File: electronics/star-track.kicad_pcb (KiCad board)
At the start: 2 copper layers, 142.2 x 61 mm, 25 parts, among them J4 AZ motor, J5 ALT motor, P1 Power in (from CB1 / J1), P2 Case: LEDs, buzzer, E-stop, P3 Hand unit (to J2), U1 L7805CV

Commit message: Drop the buzzer; colour the stripboard pictures by net
- Remove BZ1 and its GPIO from the schematic, the stripboard and the
  docs. Feedback at the mount is the two LEDs. P2 keeps five pads.
- Stripboard pictures: one colour per net for the strips and the wire
  links, fixed colours for GND, +12V, +3V3 and +5V.

Co-Authored-By: Claude Opus 5.5 <noreply@anthropic.com>
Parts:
- P2: value Case: LEDs, buzzer, E-stop -> Case: LEDs, E-stop
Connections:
- A1 pad 20: /BUZZER -> unconnected-(A1-GPIO14-Pad20)
- P2 pad 3: /BUZZER -> /EN_OUT
- P2 pad 4: /EN_OUT -> GND
- P2 pad 5: GND -> /DRV_EN
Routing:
- net unconnected-(A1-GPIO14-Pad20): track 0.00 -> 48.3 mm
- net /BUZZER: track 48.3 -> 0.00 mm

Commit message: Replace the L7805 with a DC-DC converter, add a GPS module
- U1 is now a DC-DC step-down module set to 5 V, off the board on three
  wires (pads P5). The L7805 and its heatsink are gone.
- GPS module GY-GPS6MV2 (u-blox NEO-6M) on GPIO16/17, powered from 5 V,
  wired to pads P4. It gives the time and the site to the firmware.
- Motor cables are soldered into J4, J5.
- Stripboard pictures: the notes under the board are laid out in columns.
- docs: power, GPS, pins, power budget and parts list updated.

Co-Authored-By: Claude Opus 5.5 <noreply@anthropic.com>
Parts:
- removed U1: L7805CV, Package_TO_SOT_THT:TO-220-3_Vertical
- added P4: GPS module (U2), Wire_pads, F.Cu at (191.4, 82.9)
- added P5: DC-DC module (U1), Wire_pads, F.Cu at (100.0, 90.5)
- moved W4 2.54 mm to (163.5, 98.1)
- moved W5 2.54 mm to (161.0, 87.9)
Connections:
- A1 pad 10: unconnected-(A1-GPIO17-Pad10) -> /GPS_TX
- A1 pad 9: unconnected-(A1-GPIO16-Pad9) -> /GPS_RX
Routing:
- net unconnected-(A1-GPIO17-Pad10): track 48.3 -> 0.00 mm
- net unconnected-(A1-GPIO16-Pad9): track 48.3 -> 0.00 mm
- net /GPS_TX: track 0.00 -> 48.3 mm
- net /GPS_RX: track 0.00 -> 48.3 mm

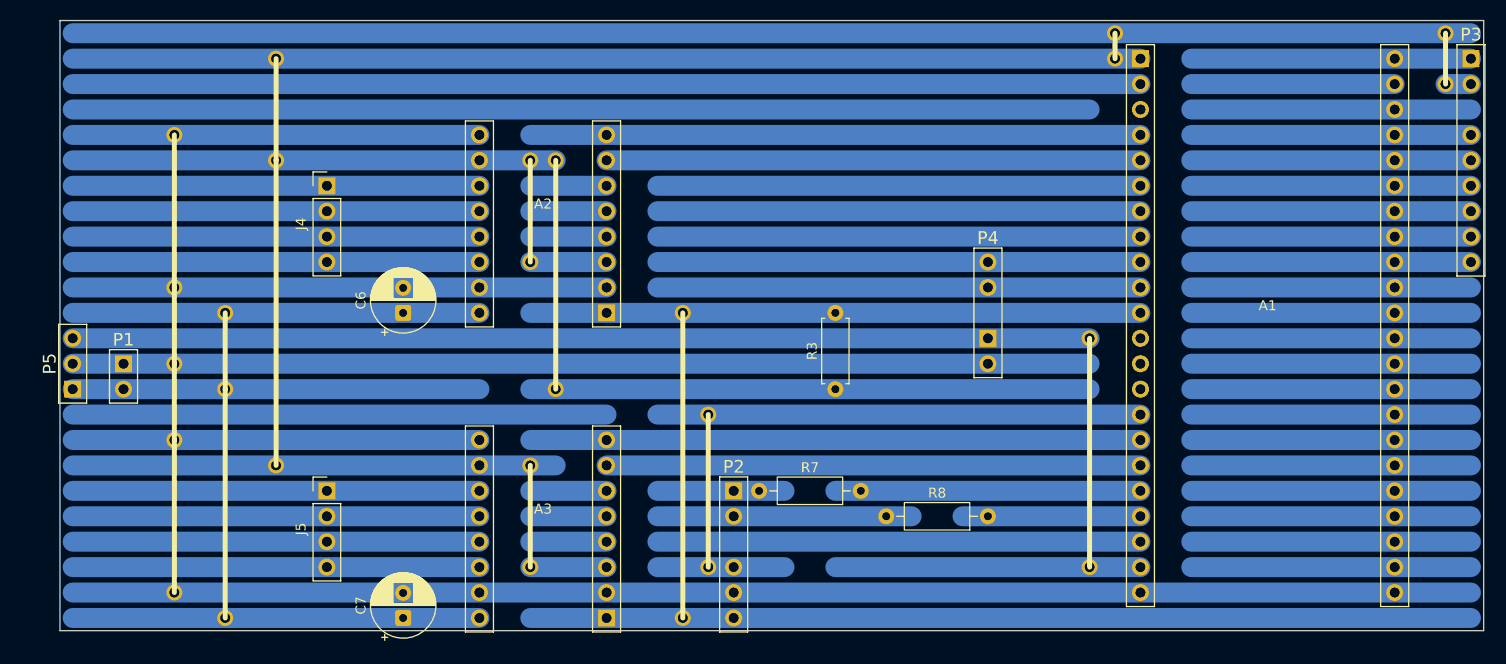
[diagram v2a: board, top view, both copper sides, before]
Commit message: Add a two-layer PCB for the electronics; move the stripboard to a subfolder
- electronics/star-track.kicad_pcb: 72 x 61 mm, two layers, through-hole
  parts only, rounded corners, four M3 holes. Laid out by function:
  motor wires and power on the left edge, drivers in the middle, the
  ESP32 board on the right with the resistors under it, hand unit and
  GPS on the right edge, LEDs and E-stop on the bottom edge (each LED
  with its own GND pad). Power input on a 5.08 mm screw terminal.
- Routed with Freerouting, GND fill on both layers except under the
  ESP32 antenna. DRC passes with no unconnected pads.
- Gerber and drill files for ordering, and renders of both sides.
- Net classes for the track widths; KiCad's default checks restored.
- ESP32 footprint courtyard limited to its two header strips.
- The stripboard moves to electronics/stripboard/.

Co-Authored-By: Claude Opus 5.5 <noreply@anthropic.com>
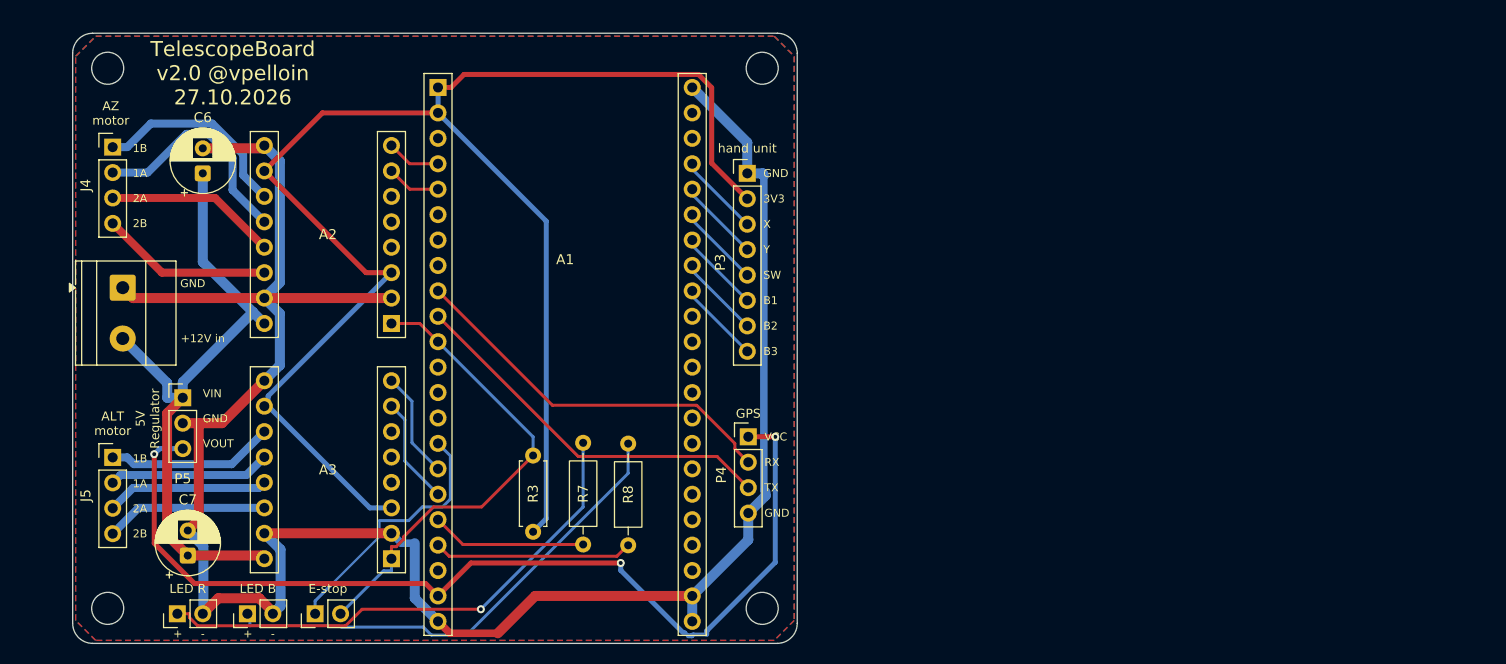
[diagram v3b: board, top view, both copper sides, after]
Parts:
- removed W1, W10, W11, W2, W3, W4, W5, W6, W7, W8, W9: Wire link, Wire_link
- added H1: MountingHole_3.2mm_M3, MountingHole:MountingHole_3.2mm_M3, F.Cu at (103.5, 63.5)
- added H2: MountingHole_3.2mm_M3, MountingHole:MountingHole_3.2mm_M3, F.Cu at (103.5, 117.5)
- added H3: MountingHole_3.2mm_M3, MountingHole:MountingHole_3.2mm_M3, F.Cu at (168.9, 63.5)
- added H4: MountingHole_3.2mm_M3, MountingHole:MountingHole_3.2mm_M3, F.Cu at (168.9, 117.5)
- added P6: Blue LED (D4), Connector_PinHeader_2.54mm:PinHeader_1x02_P2.54mm_Vertical, F.Cu at (117.5, 118.0)
- added P7: E-stop (SW2), Connector_PinHeader_2.54mm:PinHeader_1x02_P2.54mm_Vertical, F.Cu at (124.2, 118.0)
- P1: value Power in (from CB1 / J1) -> EK508V-02P; footprint Wire_pads -> TerminalBlock_Phoenix:TerminalBlock_Phoenix_MKDS-1,5-2-5.08_1x02_P5.08mm_Horizontal
- P2: value Case: LEDs, E-stop -> Red LED (D3); footprint Wire_pads -> Connector_PinHeader_2.54mm:PinHeader_1x02_P2.54mm_Vertical
- P3: value Hand unit (to J2) -> Hand unit (J2); footprint Wire_pads -> Connector_PinHeader_2.54mm:PinHeader_1x08_P2.54mm_Vertical
- P4: value GPS module (U2) -> GPS (U2); footprint Wire_pads -> Connector_PinHeader_2.54mm:PinHeader_1x04_P2.54mm_Vertical
- P5: value DC-DC module (U1) -> DC-DC 5V (U1); footprint Wire_pads -> Connector_PinHeader_2.54mm:PinHeader_1x03_P2.54mm_Vertical
- moved P3 73.2 mm to (167.4, 74.0)
- moved A1 70.2 mm to (136.5, 65.4)
- moved P2 56.9 mm to (110.5, 118.0), turned to 90 degrees
- moved R8 36.1 mm to (155.5, 111.2), turned to 90 degrees
- moved R3 33.4 mm to (146.0, 109.8)
- moved P4 29.6 mm to (167.5, 100.3)
- moved R7 28.3 mm to (151.0, 111.1), turned to 90 degrees
- moved C6 24.4 mm to (113.0, 74.0)
- moved C7 22.4 mm to (111.5, 112.2)
- moved A3 22.3 mm to (131.8, 112.5)
- moved J4 21.7 mm to (104.0, 71.4)
- moved J5 21.7 mm to (104.0, 102.4)
- moved A2 21.5 mm to (131.8, 89.0)
- moved P5 12.5 mm to (111.0, 96.4)
- moved P1 7.60 mm to (105.0, 85.4), turned to -90 degrees
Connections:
- P2 pad 2: Net-(R8-Pad2) -> GND
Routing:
- net +3V3: track 523.2 -> 162.4 mm
- net GND: track 431.8 -> 219.1 mm
- net (no net): track 154.9 -> 0.00 mm
- net /DRV_EN: track 154.9 -> 48.0 mm
- net +12V: track 121.9 -> 63.4 mm
- net /AZ_DIR: track 61.0 -> 5.40 mm
- net /ALT_DIR: track 61.0 -> 10.7 mm
- net unconnected-(A1-GPIO7-Pad7): track 48.3 -> 0.00 mm
- net unconnected-(A1-GPIO6-Pad6): track 48.3 -> 0.00 mm
- net unconnected-(A1-GPIO15-Pad8): track 48.3 -> 0.00 mm
- net unconnected-(A1-GPIO14-Pad20): track 48.3 -> 0.00 mm
- net /AZ_STEP: track 53.3 -> 5.40 mm
- net /ALT_STEP: track 53.3 -> 10.7 mm
- net Net-(R7-Pad2): track 12.7 -> 52.6 mm, vias 0 -> 1
- net /EN_OUT: track 61.0 -> 26.0 mm
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- added copper zone on B.Cu, net GND
- added copper zone on F.Cu, net GND
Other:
- board size 142.2 x 61 mm -> 72.4 x 61 mm
- board text added: "+"
- board text added: "+12V in"
- board text added: "-"
- board text added: "1A"
- board text added: "1B"
- board text added: "2A"
- board text added: "2B"
- board text added: "3V3"
- board text added: "5V Regulator"
- board text added: "ALT motor"
- board text added: "AZ motor"
- board text added: "B1"
- board text added: "B2"
- board text added: "B3"
- board text added: "E-stop"
- board text added: "GND"
- board text added: "GPS"
- board text added: "LED B"
- board text added: "LED R"
- board text added: "RX"
- board text added: "SW"
- board text added: "TX"
- board text added: "TelescopeBoard v2.0 @vpelloin 27.10.2026"
- board text added: "VCC"
- board text added: "VIN"
- board text added: "VOUT"
- board text added: "Y"
- board text added: "hand unit"
- board text removed: "1"
- board text removed: "11"
- board text removed: "16"
- board text removed: "21"
- board text removed: "26"
- board text removed: "31"
- board text removed: "36"
- board text removed: "41"
- board text removed: "46"
- board text removed: "51"
- board text removed: "56"
- board text removed: "6"
- board text removed: "A"
- board text removed: "B"
- board text removed: "C"
- board text removed: "D"
- board text removed: "E"
- board text removed: "F"
- board text removed: "G"
- board text removed: "H"
- board text removed: "I"
- board text removed: "J"
- board text removed: "K"
- board text removed: "L"
- board text removed: "M"
- board text removed: "N"
- board text removed: "O"
- board text removed: "P"
- board text removed: "Q"
- board text removed: "R"
- board text removed: "S"
- board text removed: "Star-Track - stripboard 24 x 56, component side. Strips run left-right on the back."
- board text removed: "T"
- board text removed: "U"
- board text removed: "V"
- board text removed: "W"

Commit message: Add a Schottky diode on the 5 V supply, use SMD resistors, re-route the PCB
- D5 (PMEG3005EB) between the DC-DC output and the ESP32 board's 5V pin, so
  USB and the 12 V supply can be connected at the same time.
- R3, R7, R8 as 0603 and D5 as SOD-523, for hand soldering; R8 now 330 ohm.
- PCB: C6 moved next to the azimuth driver's VM pin, new placement and
  routing, antenna keep-out with no copper, orientation labels on the driver
  sockets and the ESP32 board, silkscreen strokes of at least 0.15 mm.
- Gerbers, renders and docs updated.

Co-Authored-By: Claude Opus 5.5 <noreply@anthropic.com>
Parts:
- added D5: PMEG3005EB, Diode_SMD:D_SOD-523, F.Cu at (131.7, 116.5)
- R3: footprint Resistor_THT:R_Axial_DIN0207_L6.3mm_D2.5mm_P7.62mm_Horizontal -> Resistor_SMD:R_0603_1608Metric_Pad0.98x0.95mm_HandSolder
- R7: footprint Resistor_THT:R_Axial_DIN0207_L6.3mm_D2.5mm_P10.16mm_Horizontal -> Resistor_SMD:R_0603_1608Metric_Pad0.98x0.95mm_HandSolder
- R8: value 220 -> 330; footprint Resistor_THT:R_Axial_DIN0207_L6.3mm_D2.5mm_P10.16mm_Horizontal -> Resistor_SMD:R_0603_1608Metric_Pad0.98x0.95mm_HandSolder
- moved C6 15.1 mm to (111.5, 89.0)
- moved P1 14.5 mm to (105.3, 71.0)
- moved J4 12.5 mm to (103.5, 83.9)
- moved R3 6.17 mm to (150.5, 105.6), turned to -90 degrees
- moved R8 5.79 mm to (150.5, 114.1), turned to -90 degrees
- moved J5 2.06 mm to (103.5, 104.4)
- moved R7 1.27 mm to (150.5, 109.9), turned to -90 degrees
- moved P5 1.00 mm to (111.0, 95.4)
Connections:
- P5 pad 3: +5V -> /5V_DCDC
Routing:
- net GND: track 219.1 -> 0.00 mm
- net +5V: track 99.5 -> 53.7 mm, vias 3 -> 0
- net /5V_DCDC: track 0.00 -> 26.7 mm, vias 0 -> 1
- net +3V3: track 162.4 -> 184.5 mm, vias 0 -> 1
- net Net-(A2-2A): track 17.2 -> 33.0 mm
- net Net-(R8-Pad2): track 49.1 -> 35.5 mm
- net +12V: track 63.4 -> 55.9 mm
- net /DRV_EN: track 48.0 -> 55.0 mm, vias 0 -> 1
- net /GPS_TX: track 38.1 -> 44.9 mm
- net Net-(R7-Pad2): track 52.6 -> 47.4 mm, vias 1 -> 0
- net /LED_BLUE: track 19.9 -> 14.8 mm
- net /EN_OUT: track 26.0 -> 30.5 mm, vias 0 -> 1
- net /LED_RED: track 15.5 -> 19.6 mm
- net Net-(A2-1A): track 22.3 -> 18.8 mm, vias 0 -> 1
- net Net-(A2-2B): track 17.2 -> 20.0 mm, vias 0 -> 1
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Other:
- board text added: "DIR"
- board text added: "EN"
- board text added: "TelescopeBoard v2.0 @vpelloin 28.10.2026"
- board text added: "USB end"
- board text added: "VM"
- board text removed: "TelescopeBoard v2.0 @vpelloin 27.10.2026"
